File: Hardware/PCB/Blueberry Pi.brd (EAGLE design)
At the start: 99.1 x 64.8 mm, 172 parts, among them IC3 AT45DB161D, J1 TRANSFLASH-LOCK, J2 AUDIO_JACK_SMD, Q1 24Mhz, Q2 32kHz, X1 USB-B-S, X3 52745-2290

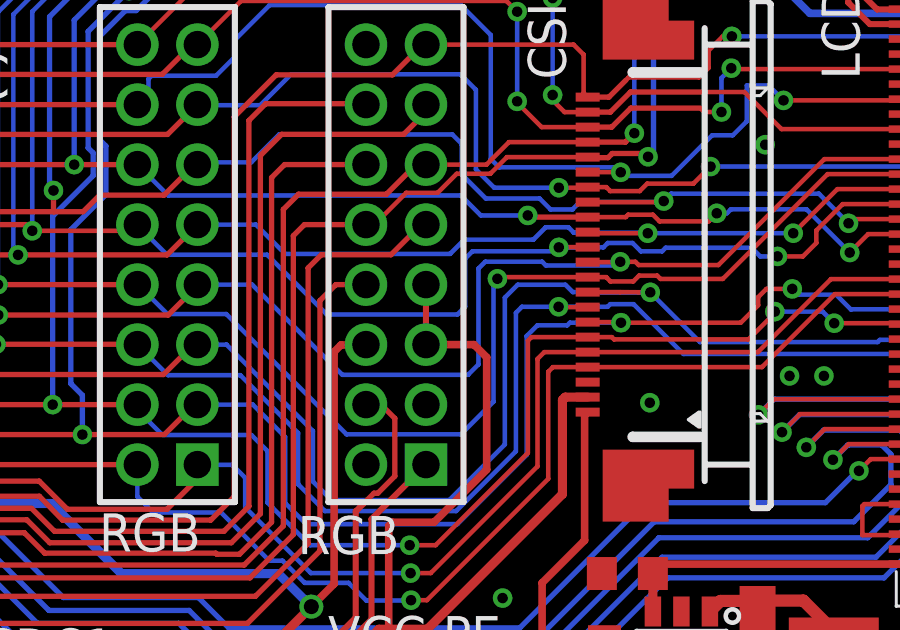
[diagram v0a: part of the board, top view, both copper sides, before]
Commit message: updated schematics
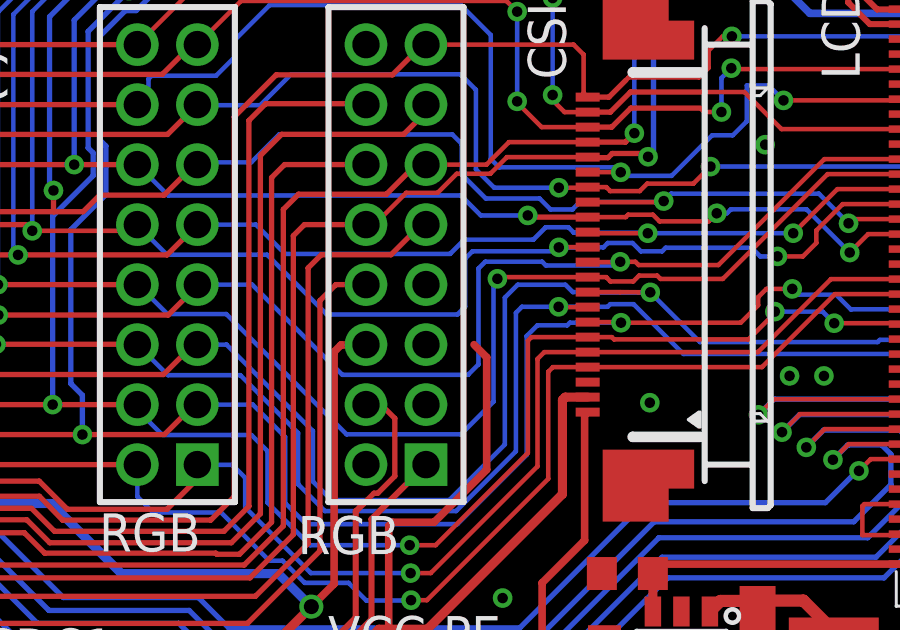
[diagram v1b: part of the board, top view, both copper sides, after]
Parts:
- U$5: value MICRO-USB-SHIELD-ZX62R-B-5P -> (none)
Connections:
- net UART2/RX renamed UART2/TX/PB0
- net UART2/TX renamed UART2/RX/PB1
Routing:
- net +3V3: track 488.9 -> 485.3 mm
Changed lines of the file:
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@@
 <drawing>
 <settings>
-<setting alwaysvectorfont="yes"/>
+<setting alwaysvectorfont="no"/>
 <setting keepoldvectorfont="yes"/>
 <setting verticaltext="up"/>
@@
 <grid distance="0.000003125" unitdist="mm" unit="mm" style="lines" multiple="1" display="yes" altdistance="5" altunitdist="mil" altunit="mil"/>
 <layers>
-<layer number="1" name="Top" color="4" fill="1" visible="yes" active="yes"/>
+<layer number="1" name="Top" color="4" fill="1" visible="no" active="yes"/>
 <layer number="2" name="Route2" color="1" fill="3" visible="no" active="no"/>
 <layer number="3" name="Route3" color="4" fill="3" visible="no" active="no"/>
@@
 <layer number="15" name="Route15" color="4" fill="6" visible="no" active="no"/>
 <layer number="16" name="Bottom" color="1" fill="1" visible="no" active="yes"/>
-<layer number="17" name="Pads" color="2" fill="1" visible="yes" active="yes"/>
-<layer number="18" name="Vias" color="2" fill="1" visible="yes" active="yes"/>
-<layer number="19" name="Unrouted" color="6" fill="1" visible="yes" active="yes"/>
+<layer number="17" name="Pads" color="2" fill="1" visible="no" active="yes"/>
+<layer number="18" name="Vias" color="2" fill="1" visible="no" active="yes"/>
+<layer number="19" name="Unrouted" color="6" fill="1" visible="no" active="yes"/>
 <layer number="20" name="Dimension" color="15" fill="1" visible="yes" active="yes"/>
-<layer number="21" name="tPlace" color="7" fill="1" visible="yes" active="yes"/>
+<layer number="21" name="tPlace" color="7" fill="1" visible="no" active="yes"/>
 <layer number="22" name="bPlace" color="7" fill="1" visible="yes" active="yes"/>
-<layer number="23" name="tOrigins" color="15" fill="1" visible="yes" active="yes"/>
+<layer number="23" name="tOrigins" color="15" fill="1" visible="no" active="yes"/>
 <layer number="24" name="bOrigins" color="15" fill="1" visible="yes" active="yes"/>
-<layer number="25" name="tNames" color="7" fill="1" visible="yes" active="yes"/>
-<layer number="26" name="bNames" color="7" fill="1" visible="yes" active="yes"/>
+<layer number="25" name="tNames" color="7" fill="1" visible="no" active="yes"/>
+<layer number="26" name="bNames" color="7" fill="1" visible="no" active="yes"/>
 <layer number="27" name="tValues" color="7" fill="1" visible="no" active="yes"/>
 <layer number="28" name="bValues" color="7" fill="1" visible="no" active="yes"/>
@@
 <layer number="41" name="tRestrict" color="4" fill="10" visible="no" active="yes"/>
 <layer number="42" name="bRestrict" color="1" fill="10" visible="no" active="yes"/>
-<layer number="43" name="vRestrict" color="2" fill="10" visible="yes" active="yes"/>
-<layer number="44" name="Drills" color="7" fill="1" visible="yes" active="yes"/>
+<layer number="43" name="vRestrict" color="2" fill="10" visible="no" active="yes"/>
+<layer number="44" name="Drills" color="7" fill="1" visible="no" active="yes"/>
 <layer number="45" name="Holes" color="7" fill="1" visible="yes" active="yes"/>
 <layer number="46" name="Milling" color="3" fill="1" visible="yes" active="yes"/>
@@
 <layer number="49" name="Reference" color="7" fill="1" visible="yes" active="yes"/>
 <layer number="50" name="dxf" color="7" fill="1" visible="no" active="no"/>
-<layer number="51" name="tDocu" color="7" fill="1" visible="yes" active="yes"/>
+<layer number="51" name="tDocu" color="7" fill="1" visible="no" active="yes"/>
 <layer number="52" name="bDocu" color="7" fill="1" visible="yes" active="yes"/>
 <layer number="53" name="tGND_GNDA" color="7" fill="1" visible="no" active="no"/>
@@
 <attribute name="VALUE" x="81.91915625" y="8.668440625" size="1.27" layer="27" rot="R270"/>
 </element>
-<element name="U$5" library="con-hirose" package="ZX62R-B-5P" value="MICRO-USB-SHIELD-ZX62R-B-5P" x="1.559859375" y="18.974234375" smashed="yes">
+<element name="U$5" library="con-hirose" package="ZX62R-B-5P" value="" x="1.559859375" y="18.974234375" smashed="yes">
 <attribute name="VALUE" x="8.544859375" y="14.529234375" size="1.27" layer="27" rot="R90"/>
 </element>
@@
 <contactref element="RN2" pad="3"/>
 <contactref element="RN2" pad="4"/>
-<contactref element="JP12" pad="5"/>
 <contactref element="RN1" pad="4"/>
 <contactref element="RN1" pad="3"/>
@@
 <wire x1="73.915578125" y1="16.938084375" x2="73.6843625" y2="16.70686875" width="0.3048" layer="1"/>
 <via x="73.6843625" y="16.70686875" extent="1-16" drill="0.35"/>
-<wire x1="75.93" y1="31.29" x2="77.53145625" y2="31.29" width="0.254" layer="1"/>
 <wire x1="77.53145625" y1="31.29" x2="77.953353125" y2="30.868103125" width="0.254" layer="1"/>
 <wire x1="77.953353125" y1="30.868103125" x2="77.953353125" y2="27.121146875" width="0.254" layer="1"/>
@@
 <wire x1="82.4303875" y1="15.701275" x2="80.613034375" y2="17.518628125" width="0.3048" layer="16"/>
 <contactref element="JP12" pad="7"/>
-<wire x1="75.93" y1="31.29" x2="75.93" y2="33.29" width="0.2032" layer="1"/>
 <wire x1="38.973084375" y1="37.601671875" x2="38.900978125" y2="37.506646875" width="0.1778" layer="16"/>
 <wire x1="38.900978125" y1="37.506646875" x2="38.822165625" y2="37.4027875" width="0.1778" layer="16"/>
@@
 <wire x1="11.04538125" y1="23.75808125" x2="16.061446875" y2="23.75808125" width="0.3048" layer="16"/>
 <wire x1="16.061446875" y1="23.75808125" x2="16.16049375" y2="23.857128125" width="0.3048" layer="16"/>
+<contactref element="JP12" pad="5"/>
+<wire x1="75.93" y1="31.29" x2="75.93" y2="33.29" width="0" layer="19" extent="1-1"/>
+<wire x1="77.53145625" y1="31.29" x2="75.93" y2="31.29" width="0" layer="19" extent="1-1"/>
 </signal>
 <signal name="+3V3A">
@@
 <wire x1="27.64580625" y1="29.86234375" x2="27.701875" y2="29.86234375" width="0.1778" layer="16"/>
 </signal>
-<signal name="UART2/RX">
+<signal name="UART2/TX/PB0">
 <contactref element="U$1" pad="39"/>
 <contactref element="JP1" pad="18"/>
@@
 <wire x1="9.871340625" y1="22.696259375" x2="16.1900875" y2="22.696259375" width="0.1524" layer="16"/>
 </signal>
-<signal name="UART2/TX">
+<signal name="UART2/RX/PB1">
 <contactref element="U$1" pad="40"/>
 <contactref element="JP1" pad="16"/>
